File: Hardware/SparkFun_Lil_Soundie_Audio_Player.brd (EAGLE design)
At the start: 25.4 x 55.9 mm, 66 parts, among them J1 Audio Jack, J2 AMP FCI 10103594-0001LF, U2 VS1000, U3 4MB Flash, Y1 12MHz

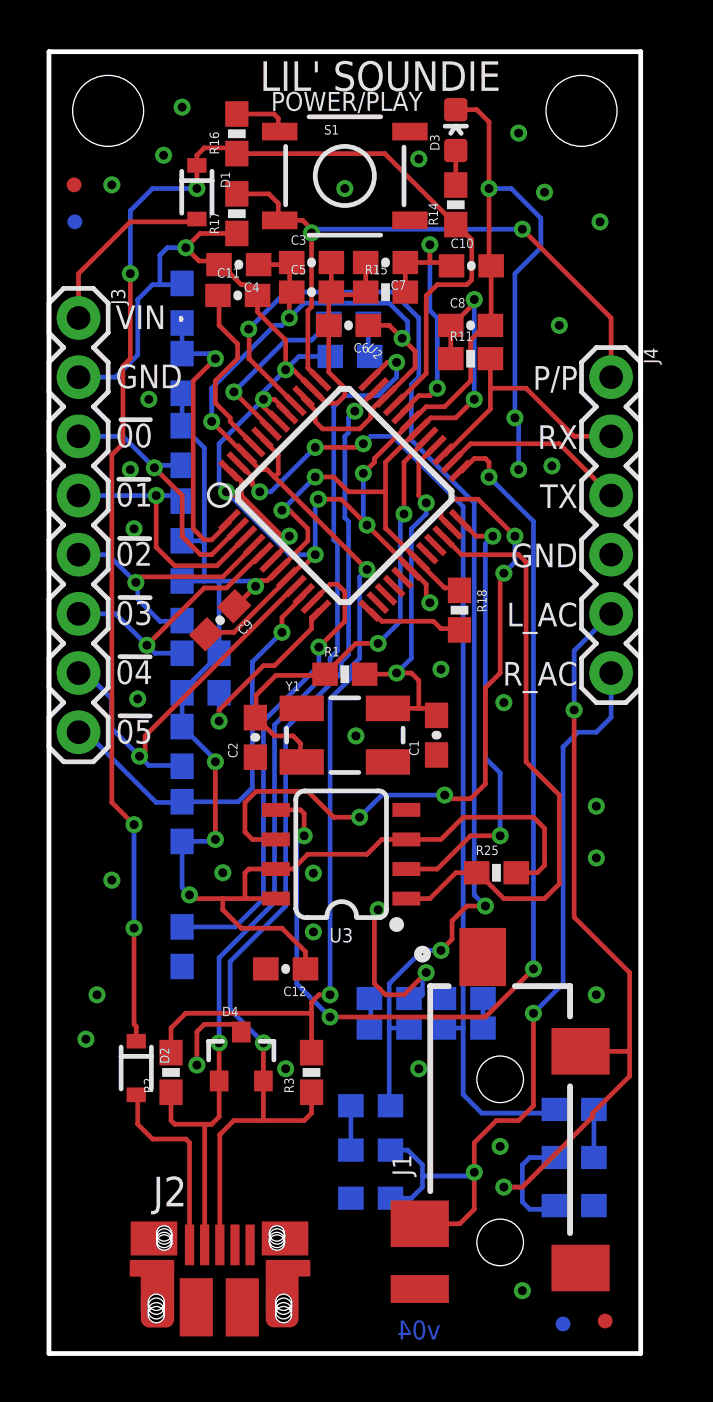
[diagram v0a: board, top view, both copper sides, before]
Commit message: Updated design: active high input pins. Cleaned up schematic and layout
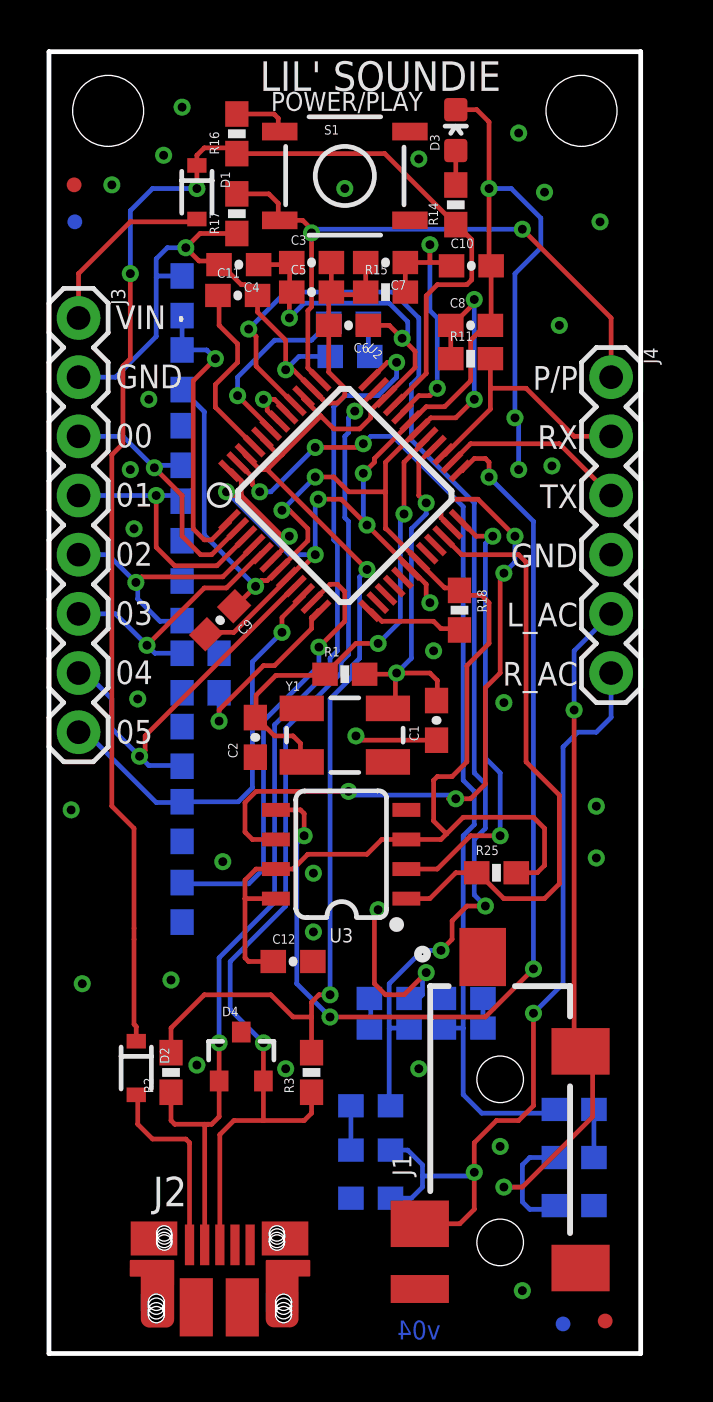
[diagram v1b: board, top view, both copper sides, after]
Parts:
- R19, R20, R21, R22, R23: value 100k -> 4.7k; device SparkFun-Resistors:0603-RES -> SparkFun-Resistors:0603
- R24: value 100k -> 3.9k; device SparkFun-Resistors:0603-RES -> SparkFun-Resistors:0603
- moved R26 1.91 mm to (5.71, 19.4), turned to 270 degrees
- moved C1 0.64 mm to (16.6, 27.2)
- moved C12 0.45 mm to (10.5, 16.8), turned to 0 degrees
- moved C17 0.32 mm to (5.71, 45.4)
- moved R12 0.16 mm to (5.71, 42.2)
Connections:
- net DVDD: no longer R13.2, R19.2, R20.2, R21.2, R22.2, R23.2, R24.2
- net GND: now also R19.2, R20.2, R21.2, R22.2, R23.2, R24.2, R26.2; no longer R26.1
- net IO_06: now also R26.1; no longer R26.2
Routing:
- net DVDD: track 87.4 -> 77.3 mm, vias 8 -> 5
- net GND: track 117.9 -> 111.4 mm
- net AVDD: track 68.1 -> 63.0 mm, vias 5 -> 4
- net L_AC: track 36.5 -> 33.1 mm
- net IO_06: track 20.5 -> 19.0 mm
- net VHIGH: vias 4 -> 2

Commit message: Fixed trace issue on IO7
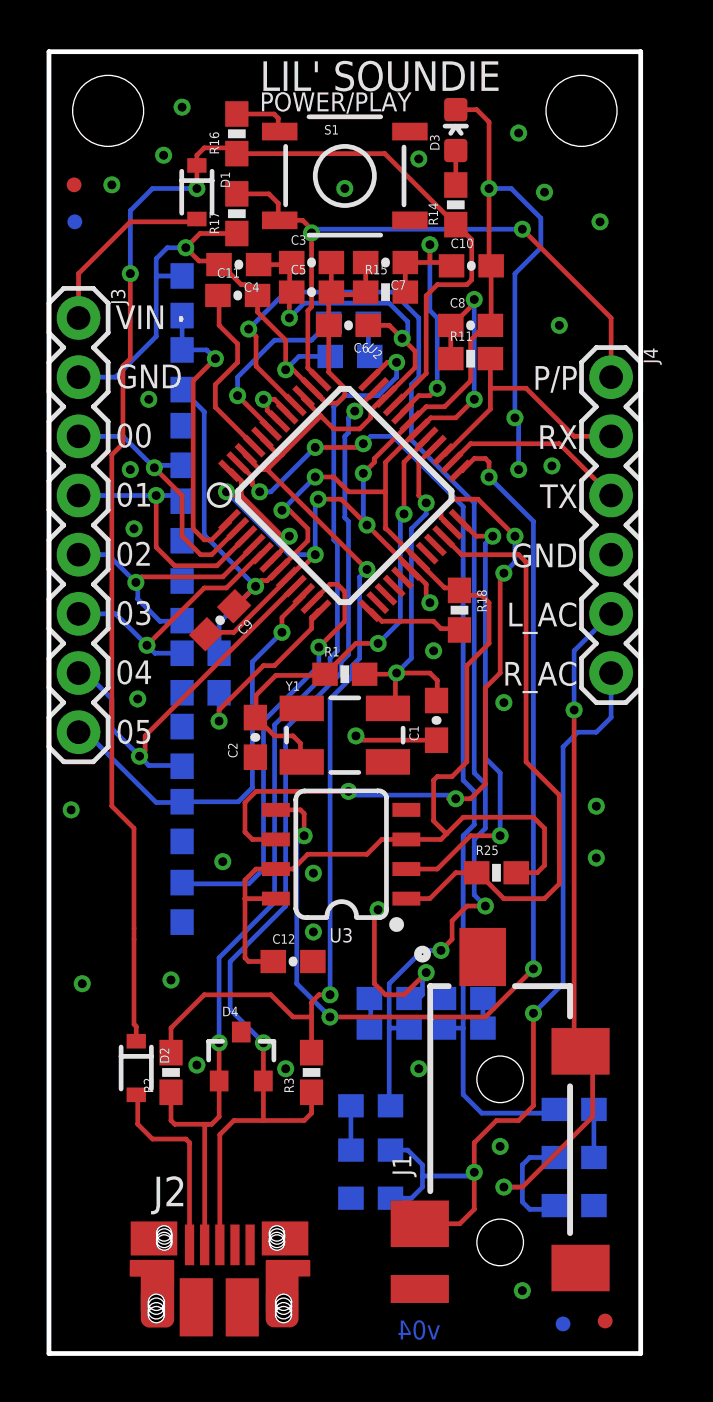
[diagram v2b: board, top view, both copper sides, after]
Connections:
- net DVDD: now also R13.2
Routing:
- net DVDD: track 77.3 -> 80.8 mm
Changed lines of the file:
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@@
 <setting verticaltext="up"/>
 </settings>
-<grid distance="0.00625" unitdist="inch" unit="inch" style="lines" multiple="1" display="yes" altdistance="0.01" altunitdist="mm" altunit="mm"/>
+<grid distance="0.025" unitdist="inch" unit="inch" style="lines" multiple="1" display="yes" altdistance="0.01" altunitdist="mm" altunit="mm"/>
 <layers>
 <layer number="1" name="Top" color="4" fill="1" visible="yes" active="yes"/>
@@
 <layer number="45" name="Holes" color="7" fill="1" visible="no" active="yes"/>
 <layer number="46" name="Milling" color="3" fill="1" visible="no" active="yes"/>
-<layer number="47" name="Measures" color="7" fill="1" visible="no" active="yes"/>
+<layer number="47" name="Measures" color="7" fill="1" visible="yes" active="yes"/>
 <layer number="48" name="Document" color="7" fill="1" visible="no" active="yes"/>
 <layer number="49" name="Reference" color="7" fill="1" visible="no" active="yes"/>
@@
 <text x="2.8575" y="38.89375" size="1.016" layer="21" font="vector" ratio="20">00</text>
 <text x="2.8575" y="43.97375" size="1.016" layer="21" font="vector" ratio="20">VIN</text>
-<text x="9.525" y="53.34" size="0.8128" layer="21" font="vector" ratio="15">POWER/PLAY</text>
+<text x="9.045" y="53.32" size="0.8128" layer="21" font="vector" ratio="15">POWER/PLAY</text>
 <text x="6.12775" y="54.1655" size="1.27" layer="22" font="vector" ratio="15" rot="MR180">LIL' SOUNDIE</text>
 <text x="4.95375" y="43.97375" size="0.889" layer="22" font="vector" ratio="15" rot="MR0">VIN</text>
@@
 <wire x1="16.51" y1="24.60625" x2="16.51" y2="22.86" width="0.2032" layer="1"/>
 <wire x1="16.51" y1="22.86" x2="17.065625" y2="22.304375" width="0.2032" layer="1"/>
+<contactref element="R13" pad="2"/>
+<wire x1="7.3025" y1="30.06" x2="7.3025" y2="31.365" width="0.2032" layer="16"/>
+<wire x1="7.3025" y1="31.365" x2="8.86875" y2="32.93125" width="0.2032" layer="16"/>
 </signal>
 <signal name="IO_05">

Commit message: Updated per QC review
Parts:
- D1, D2: value BAT20J -> 1A/23V/620mV
- FD1, FD2, FD3, FD4: device SparkFun-Aesthetics:MICRO-FIDUCIAL -> SparkFun-Aesthetics:FIDUCIAL-MICRO
- LOGO6: device SparkFun-Aesthetics:SFE_LOGO_NAME_FLAME_.2 -> SparkFun-Aesthetics:SFE_LOGO_NAME_FLAME_.1
- U2: value VS1000 -> VS1000D; device SparkFun-DigitalIC:LQFP-48 -> SparkFun-IC-Conversion:LQFP-48
- moved LOGO1 15.5 mm to (12.7, 37.5)
- moved LOGO6 13.1 mm to (12.4, 6.51)
- moved LOGO2 5.75 mm to (16.5, 22.2)
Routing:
- net N$19: track 1.48 -> 2.51 mm

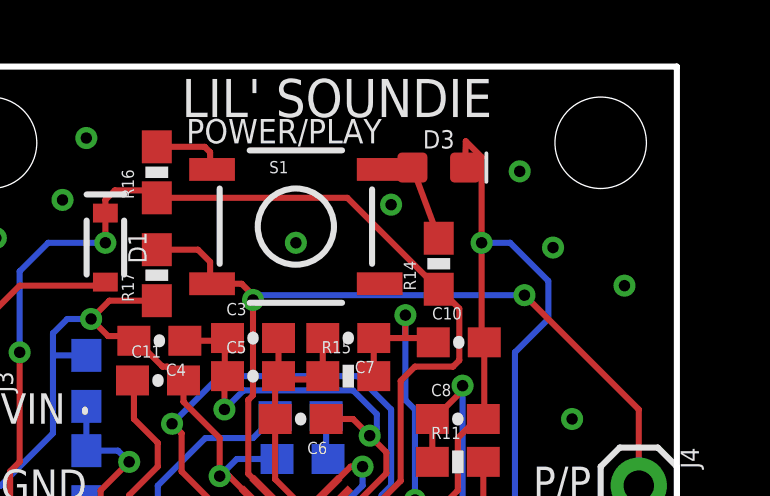
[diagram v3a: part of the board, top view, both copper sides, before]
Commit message: Moving LED
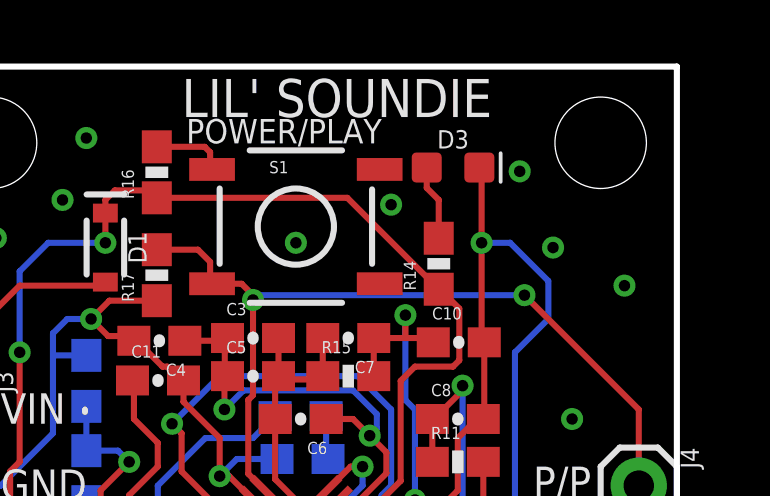
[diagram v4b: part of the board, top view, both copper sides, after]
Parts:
- moved D3 0.48 mm to (17.9, 52.5)
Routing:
- net GND: track 111.3 -> 109.7 mm
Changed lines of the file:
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@@
 <attribute name="PROD_ID" value="DIO-11623" x="3.7465" y="12.2555" size="1.778" layer="27" font="vector" ratio="15" rot="R270" display="off"/>
 </element>
-<element name="D3" library="SparkFun-LED" package="LED-0603" value="RED" x="17.4625" y="52.5145">
-<attribute name="PROD_ID" value="DIO-00819" x="17.4625" y="52.5145" size="1.778" layer="27" font="vector" ratio="15" display="off"/>
+<element name="D3" library="SparkFun-LED" package="LED-0603" value="RED" x="17.93875" y="52.5145">
+<attribute name="PROD_ID" value="DIO-00819" x="17.93875" y="52.5145" size="1.778" layer="27" font="vector" ratio="15" display="off"/>
 </element>
 <element name="R4" library="SparkFun-Resistors" package="0603-RES" value="10K" x="13.81125" y="6.6675" rot="MR180">
@@
 <wire x1="13.48375" y1="45.44875" x2="13.59625" y2="45.56125" width="0.2032" layer="1"/>
 <wire x1="13.59625" y1="46.83125" x2="13.59625" y2="45.56125" width="0.2032" layer="1"/>
-<wire x1="18.3395" y1="52.5145" x2="18.3635" y2="53.3915" width="0.2032" layer="1"/>
-<wire x1="18.3635" y1="53.3915" x2="18.89125" y2="52.86375" width="0.2032" layer="1"/>
 <wire x1="18.89125" y1="52.86375" x2="18.89125" y2="50.00625" width="0.2032" layer="1"/>
 <wire x1="18.89125" y1="50.00625" x2="18.89125" y2="46.7775" width="0.2032" layer="1"/>
@@
 <contactref element="D3" pad="A"/>
 <contactref element="R14" pad="2"/>
-<wire x1="16.5855" y1="52.5145" x2="17.4625" y2="50.15775" width="0.2032" layer="1"/>
+<wire x1="17.06175" y1="52.5145" x2="17.06175" y2="51.83575" width="0.2032" layer="1"/>
+<wire x1="17.06175" y1="51.83575" x2="17.4625" y2="51.435" width="0.2032" layer="1"/>
+<wire x1="17.4625" y1="51.435" x2="17.4625" y2="50.15775" width="0.2032" layer="1"/>
 </signal>
 <signal name="N$3">

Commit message: Updating Silk
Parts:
- removed LOGO6: SFE_LOGO_NAME_FLAME.1_INCH, SparkFun-Aesthetics:SFE_LOGO_NAME_FLAME_.1
- removed R16: 68.1k, SparkFun-Resistors:0603-RES
- added U$1: (no value), SparkFun-Aesthetics:SFE_LOGO_FLAME_.1
- LOGO2: value SFE_LOGO_FLAME.4_INCH -> SFE_LOGO_NAME.1_INCH; device SparkFun-Aesthetics:SFE_LOGO_FLAME_.4 -> SparkFun-Aesthetics:SFE_LOGO_NAME_.1
- R19, R20, R21, R22, R23: value 4.7k -> 100k
- R24: value 3.9k -> 100k
- moved LOGO2 12.8 mm to (19.2, 34.8)
- moved LOGO1 7.62 mm to (12.9, 29.8)
- moved R17 1.27 mm to (8.06, 50.2)
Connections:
- removed net N$16: R16.2, S1.1
- new net N$8: R11.1
- net DVDD: now also R11.2; no longer R11.1
- net RX: no longer R11.2
- net VHIGH: now also S1.1; no longer R16.1
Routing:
- net GND: track 109.7 -> 103.7 mm
- net VHIGH: track 64.1 -> 67.9 mm
- net PWRBTN: track 28.0 -> 30.6 mm
- net N$16: track 2.45 -> 0.00 mm
- net RX: track 11.0 -> 8.82 mm
- net DVDD: track 80.8 -> 81.4 mm
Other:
- board text added: "LITTLE SOUNDIE"
- board text added: "PB"
- board text added: "v10"
- board text removed: "AUDIO PLAYER"
- board text removed: "LIL' SOUNDIE"
- board text removed: "v04"
